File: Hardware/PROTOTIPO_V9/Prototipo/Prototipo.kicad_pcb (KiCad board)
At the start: 2 copper layers, 3 parts

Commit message: Planteo de PCBs
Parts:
- removed REF**: ILI9341, footprints_proyecto:ILI9341
- removed REF**: W5500_ETHERNET_SHIELD, footprints_proyecto:W5500_ETHERNET_SHIELD
- removed REF**: BluePill, footprints_proyecto:YAAJ_BluePill_1
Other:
- board outline added: 204.9 x 224.8 mm
- board text added: "PCB BACK"
- board text added: "PCB FRONT"
- board text added: "Trabajar con grilla 2,54 mm"

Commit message: fp definitivos - Planteo de PCB con componentes
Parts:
- added C1: 100n, Capacitor_THT:CP_Radial_Tantal_D4.5mm_P5.00mm, F.Cu at (214.7, 84.8)
- added C2: 10u, Capacitor_THT:CP_Radial_D5.0mm_P2.50mm, F.Cu at (223.6, 83.8)
- added C3: 10u, Capacitor_THT:CP_Radial_D5.0mm_P2.50mm, F.Cu at (229.7, 115.1)
- added C4: 10u, Capacitor_THT:CP_Radial_D5.0mm_P2.50mm, F.Cu at (246.4, 95.4)
- added J1: Screw_Terminal_01x02, TerminalBlock:TerminalBlock_Xinya_XY308-2.54-2P_1x02_P2.54mm_Horizontal, F.Cu at (165.1, 121.9)
- added J4: Conn_01x10, Connector_PinSocket_2.54mm:PinSocket_2x05_P2.54mm_Vertical, F.Cu at (154.9, 190.5)
- added J5: Conn_01x10, Connector_PinSocket_2.54mm:PinSocket_2x05_P2.54mm_Vertical, F.Cu at (190.5, 86.4)
- added J6: Conn_01x01, Connector_PinHeader_2.54mm:PinHeader_1x01_P2.54mm_Vertical, F.Cu at (237.2, 124.5)
- added J7: Conn_01x01, Connector_PinHeader_2.54mm:PinHeader_1x01_P2.54mm_Vertical, F.Cu at (241.8, 124.5)
- added J8: Conn_01x01, Connector_PinHeader_2.54mm:PinHeader_1x01_P2.54mm_Vertical, F.Cu at (246.4, 124.5)
- added PS1: HLK-5M05, Converter_ACDC:Converter_ACDC_Hi-Link_HLK-5Mxx, F.Cu at (173.7, 50.4)
- added R1: 100, Resistor_THT:R_Axial_DIN0207_L6.3mm_D2.5mm_P10.16mm_Horizontal, F.Cu at (96.2, 249.7)
- added R10: 10k, Resistor_THT:R_Axial_DIN0207_L6.3mm_D2.5mm_P10.16mm_Horizontal, F.Cu at (132.7, 249.7)
- added R11: 10k, Resistor_THT:R_Axial_DIN0207_L6.3mm_D2.5mm_P10.16mm_Horizontal, F.Cu at (136.7, 249.7)
- added R12: 10k, Resistor_THT:R_Axial_DIN0207_L6.3mm_D2.5mm_P10.16mm_Horizontal, F.Cu at (140.8, 249.7)
- added R13: 10k, Resistor_THT:R_Axial_DIN0207_L6.3mm_D2.5mm_P10.16mm_Horizontal, F.Cu at (194.7, 128.2)
- added R14: 10k, Resistor_THT:R_Axial_DIN0207_L6.3mm_D2.5mm_P10.16mm_Horizontal, F.Cu at (215.9, 113.8)
- added R15: 10K, Resistor_THT:R_Axial_DIN0207_L6.3mm_D2.5mm_P10.16mm_Horizontal, F.Cu at (215.9, 117.9)
- added R16: 100, Resistor_THT:R_Axial_DIN0207_L6.3mm_D2.5mm_P10.16mm_Horizontal, F.Cu at (215.9, 121.9)
- added R17: 10k, Resistor_THT:R_Axial_DIN0207_L6.3mm_D2.5mm_P10.16mm_Horizontal, F.Cu at (243.3, 102.6)
- added R18: 10K, Resistor_THT:R_Axial_DIN0207_L6.3mm_D2.5mm_P10.16mm_Horizontal, F.Cu at (243.3, 106.7)
- added R2: 4k7, Resistor_THT:R_Axial_DIN0207_L6.3mm_D2.5mm_P10.16mm_Horizontal, F.Cu at (100.3, 249.7)
- added R3: 4k7, Resistor_THT:R_Axial_DIN0207_L6.3mm_D2.5mm_P10.16mm_Horizontal, F.Cu at (104.3, 249.7)
- added R4: 4k7, Resistor_THT:R_Axial_DIN0207_L6.3mm_D2.5mm_P10.16mm_Horizontal, F.Cu at (108.4, 249.7)
- added R5: 4k7, Resistor_THT:R_Axial_DIN0207_L6.3mm_D2.5mm_P10.16mm_Horizontal, F.Cu at (112.4, 249.7)
- added R6: 4k7, Resistor_THT:R_Axial_DIN0207_L6.3mm_D2.5mm_P10.16mm_Horizontal, F.Cu at (116.5, 249.7)
- added R7: 4k7, Resistor_THT:R_Axial_DIN0207_L6.3mm_D2.5mm_P10.16mm_Horizontal, F.Cu at (120.5, 249.7)
- added R8: 10k, Resistor_THT:R_Axial_DIN0207_L6.3mm_D2.5mm_P10.16mm_Horizontal, F.Cu at (124.6, 249.7)
- added R9: 10k, Resistor_THT:R_Axial_DIN0207_L6.3mm_D2.5mm_P10.16mm_Horizontal, F.Cu at (128.6, 249.7)
- added U1: YAAJ_BluePill_Part_Like_SWD_Breakout, footprints_proyecto:YAAJ_BluePill_1, F.Cu at (269.2, 76.2)
- added U10: ADS1115IDGS, footprints_proyecto:MODULE_ADS1115, F.Cu at (199.4, 114.5)
- added U2: zmpt101b, footprints_proyecto:MODULE_ZMPT101B, F.Cu at (163.8, 101.6)
- added U5: LD1117V33, Package_TO_SOT_THT:TO-220-3_Vertical, F.Cu at (210.8, 73.7)
- added U6: 3013, footprints_proyecto:MODULE_3013, F.Cu at (238.8, 58.4)
- added U7: KY-040, footprints_proyecto:MODULE_KY-040, F.Cu at (175.3, 177.8)
- added U8: W5500_ETHERNET_SHIELD, footprints_proyecto:W5500_ETHERNET_SHIELD, F.Cu at (94.0, 118.4)
- added U9: CR2013-MI2120, Display:CR2013-MI2120, F.Cu at (104.9, 235.4)
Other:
- board size 204.9 x 224.8 mm -> 204.9 x 223.9 mm

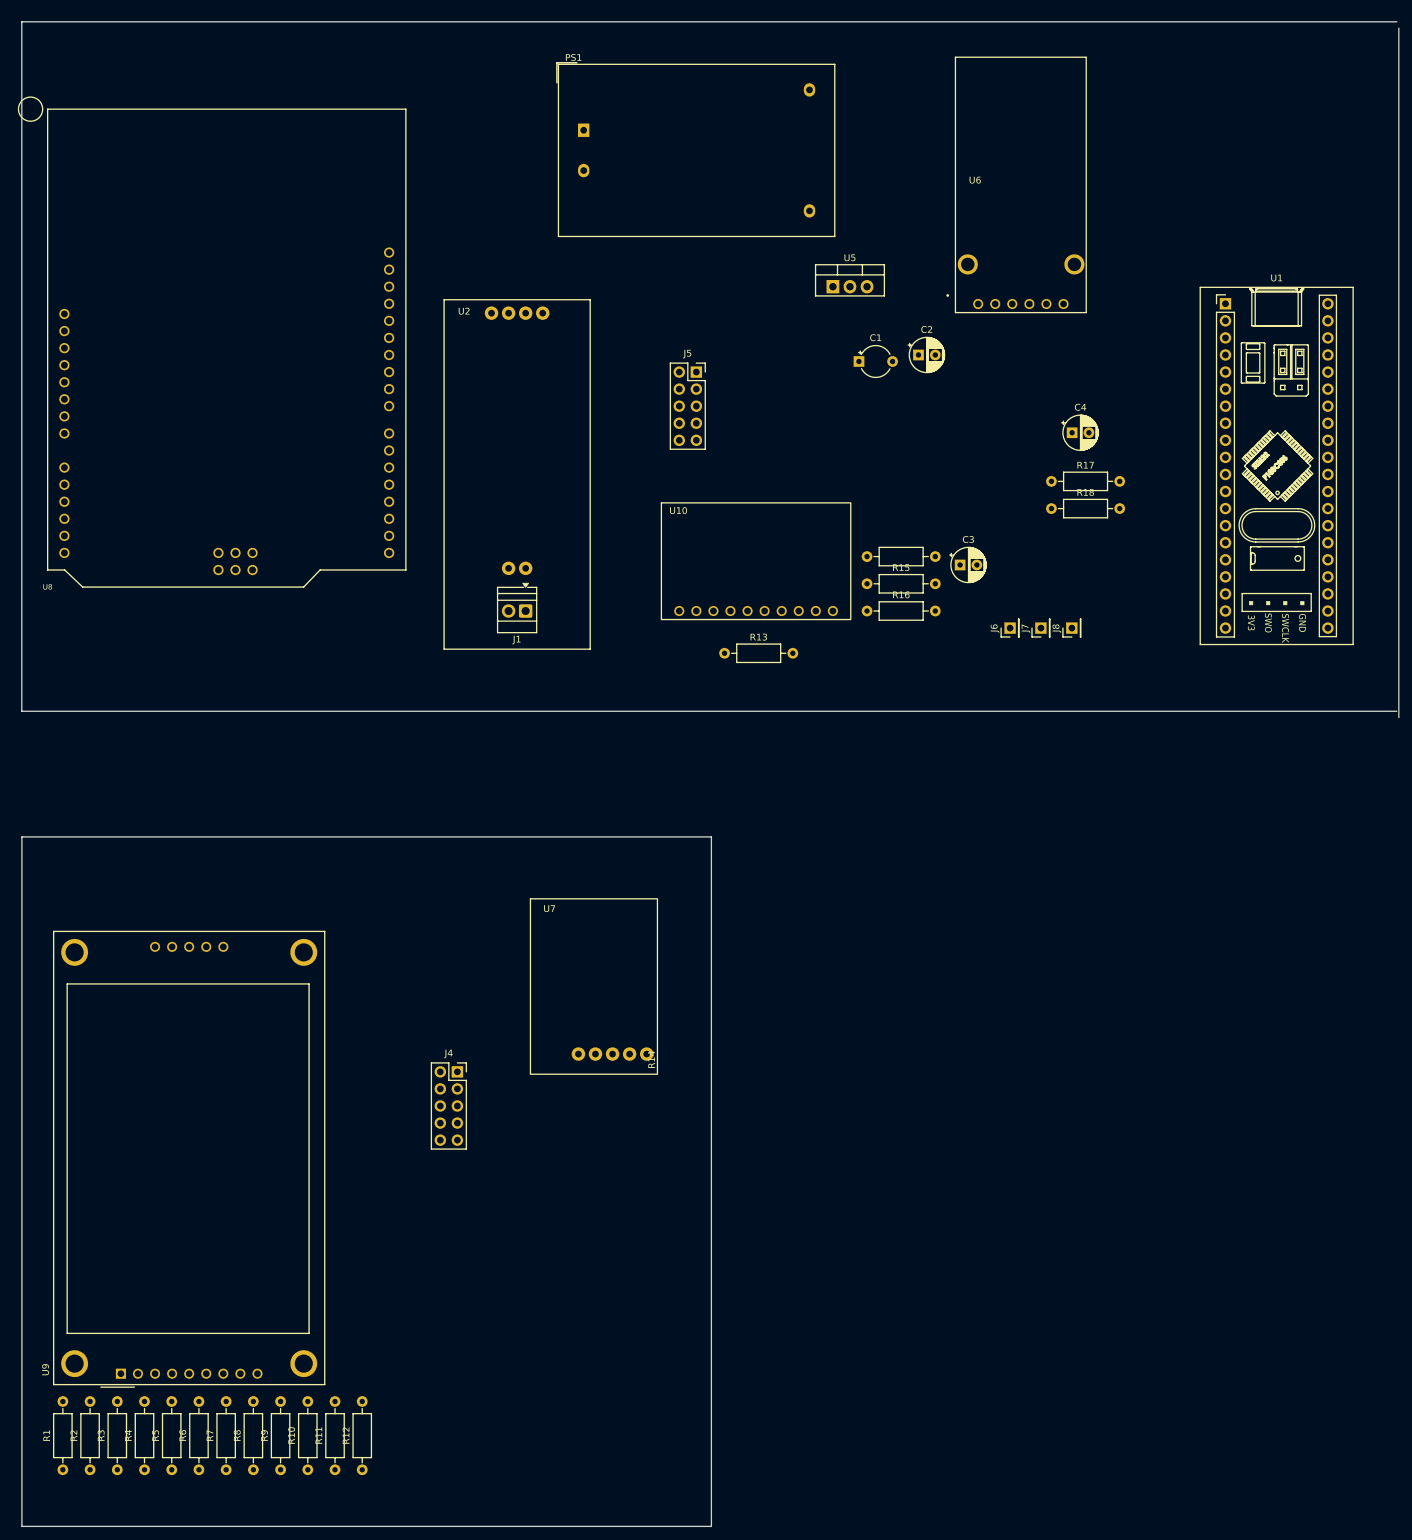
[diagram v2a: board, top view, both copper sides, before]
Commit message: Ruteo de PCB Superior
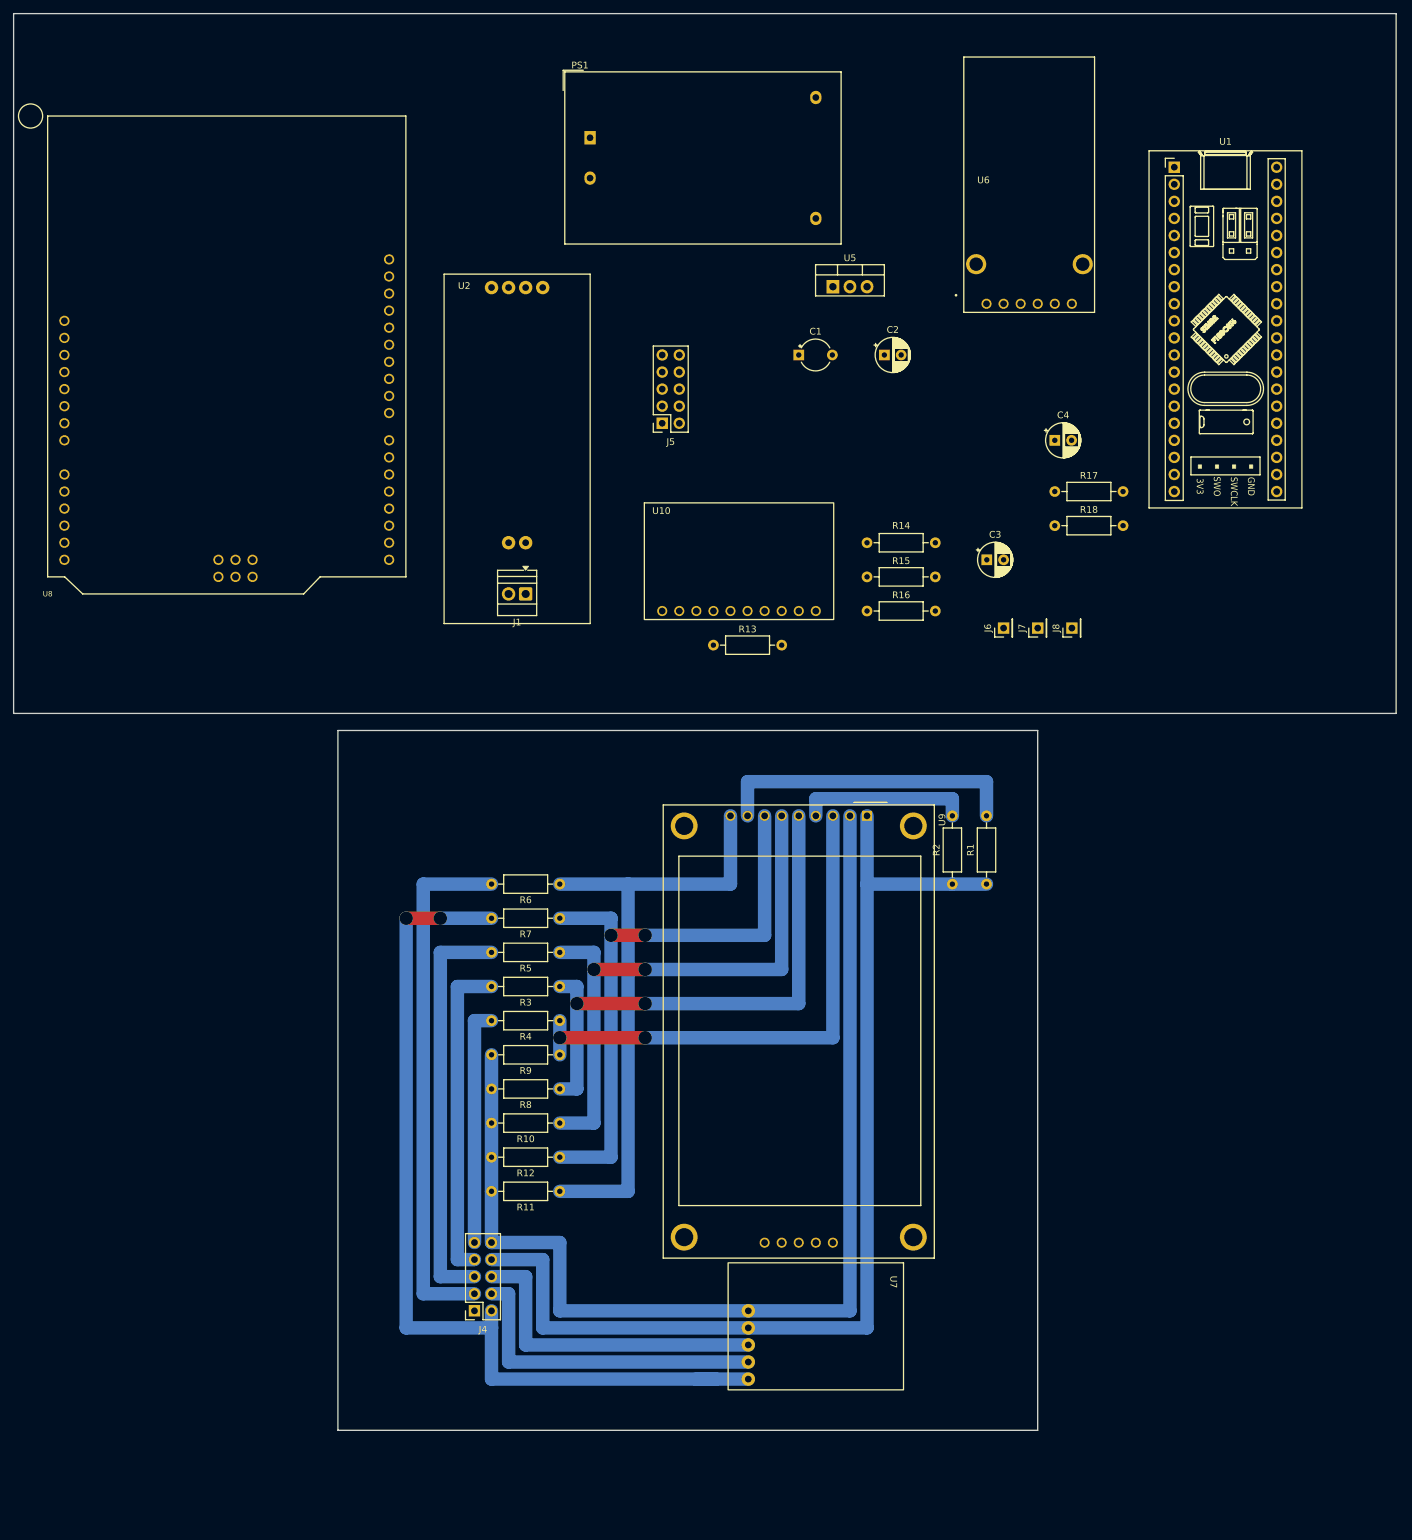
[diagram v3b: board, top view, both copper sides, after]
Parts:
- moved R1 162.8 mm to (233.7, 162.6)
- moved R2 155.1 mm to (228.6, 162.6)
- moved U9 138.6 mm to (215.9, 152.4), turned to -90 degrees
- moved R6 102.4 mm to (170.2, 162.6), turned to 180 degrees
- moved R3 97.5 mm to (170.2, 177.8), turned to 180 degrees
- moved R5 96.2 mm to (170.2, 172.7), turned to 180 degrees
- moved R7 95.9 mm to (170.2, 167.6), turned to 180 degrees
- moved R4 91.0 mm to (170.2, 182.9), turned to 180 degrees
- moved R9 74.4 mm to (170.2, 188.0), turned to 180 degrees
- moved R8 72.7 mm to (170.2, 193.0), turned to 180 degrees
- moved R10 63.8 mm to (170.2, 198.1), turned to 180 degrees
- moved U7 60.4 mm to (208.3, 228.4), turned to -90 degrees
- moved R12 55.0 mm to (170.2, 203.2), turned to 180 degrees
- moved R11 53.3 mm to (170.2, 208.3), turned to 180 degrees
- moved J4 35.7 mm to (157.5, 226.1), turned to 180 degrees
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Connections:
- J4 pad 1: +5V -> unconnected-(J4-Pin_1-Pad1)
- J4 pad 2: /PCB2CONNECTION/ENC_SW -> /PCB2CONNECTION/CLK
- J4 pad 3: /PCB2CONNECTION/ENC_DT -> /PCB2CONNECTION/LCD_MISO
- J4 pad 4: /PCB2CONNECTION/ENC_CLK -> /PCB2CONNECTION/ENC_DT
- J4 pad 5: unconnected-(J4-Pin_5-Pad5) -> /PCB2CONNECTION/LCD_MOSI
- J4 pad 6: /PCB2CONNECTION/LCD_CS -> /PCB2CONNECTION/ENC_SW
- J4 pad 8: /PCB2CONNECTION/LCD_MISO -> +5V
- J4 pad 9: /PCB2CONNECTION/LCD_MOSI -> /PCB2CONNECTION/LCD_CS
- J5 pad 1: +5V -> unconnected-(J5-Pin_1-Pad1)
- J5 pad 2: /PCB2CONNECTION/BUS_ENC_SW -> /PCB2CONNECTION/BUS_ENC_CLK
- J5 pad 3: /PCB2CONNECTION/BUS_ENC_DT -> MISO
- J5 pad 4: /PCB2CONNECTION/BUS_ENC_CLK -> /PCB2CONNECTION/BUS_ENC_DT
- J5 pad 5: unconnected-(J5-Pin_5-Pad5) -> MOSI
- J5 pad 6: /PCB2CONNECTION/BUS_LCD_CS -> /PCB2CONNECTION/BUS_ENC_SW
- J5 pad 8: MISO -> +5V
- J5 pad 9: MOSI -> /PCB2CONNECTION/BUS_LCD_CS
- R7 pad 2: /PCB2CONNECTION/ENC_CLK -> /PCB2CONNECTION/CLK
- U7 pad CLK: /PCB2CONNECTION/ENC_CLK -> /PCB2CONNECTION/CLK
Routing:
- net GND: track 0.00 -> 165.1 mm
- net +5V: track 0.00 -> 160.0 mm
- net /PCB2CONNECTION/CLK: track 0.00 -> 137.6 mm, vias 0 -> 2
- net Net-(U9-SCK): track 0.00 -> 91.4 mm, vias 0 -> 2
- net Net-(U9-MISO): track 0.00 -> 91.4 mm
- net Net-(U9-MOSI): track 0.00 -> 86.4 mm, vias 0 -> 2
- net Net-(U9-D/~{C}): track 0.00 -> 81.3 mm, vias 0 -> 2
- net Net-(U9-~{CS}): track 0.00 -> 78.7 mm, vias 0 -> 2
- net /PCB2CONNECTION/LCD_MISO: track 0.00 -> 78.7 mm
- net /PCB2CONNECTION/LCD_MOSI: track 0.00 -> 61.0 mm
- net /PCB2CONNECTION/ENC_SW: track 0.00 -> 48.4 mm
- net /PCB2CONNECTION/ENC_DT: track 0.00 -> 48.4 mm
- net /PCB2CONNECTION/LCD_DC: track 0.00 -> 48.3 mm
- net Net-(U9-LED): track 0.00 -> 45.7 mm
- net /PCB2CONNECTION/LCD_CS: track 0.00 -> 35.6 mm
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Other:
- board size 204.9 x 223.9 mm -> 205.7 x 210.8 mm
- board text added: "+5V"
- board text added: "CLK"
- board text added: "CS"
- board text added: "DC"
- board text added: "DT"
- board text added: "GND"
- board text added: "MISO"
- board text added: "MOSI"
- board text added: "SW"
- board text added: "Trabajar con grilla 2,54 mm, curvas a 90°, en capa back"
- board text removed: "Trabajar con grilla 2,54 mm"

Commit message: Migración de sch a BlackPill
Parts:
- removed R1: 100, Resistor_THT:R_Axial_DIN0207_L6.3mm_D2.5mm_P10.16mm_Horizontal
- removed R10, R11, R12, R8, R9: 10k, Resistor_THT:R_Axial_DIN0207_L6.3mm_D2.5mm_P10.16mm_Horizontal
- removed R2, R3, R4, R5, R6, R7: 4k7, Resistor_THT:R_Axial_DIN0207_L6.3mm_D2.5mm_P10.16mm_Horizontal
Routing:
- net GND: track 165.1 -> 144.8 mm
- net Net-(U9-D/~{C}): track 81.3 -> 61.0 mm, vias 2 -> 1
- net Net-(U9-~{CS}): track 78.7 -> 73.7 mm, vias 2 -> 1
- net /PCB2CONNECTION/LCD_CS: track 35.6 -> 33.0 mm

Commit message: Shc final y ruteo de PCB
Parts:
- removed C4: 10u, Capacitor_THT:CP_Radial_D5.0mm_P2.50mm
- removed R13, R17: 10k, Resistor_THT:R_Axial_DIN0207_L6.3mm_D2.5mm_P10.16mm_Horizontal
- removed R18: 10K, Resistor_THT:R_Axial_DIN0207_L6.3mm_D2.5mm_P10.16mm_Horizontal
- removed U1: YAAJ_BluePill_Part_Like_SWD_Breakout, footprints_proyecto:YAAJ_BluePill_1
- added JP1: Jumper_2_Bridged, Connector_PinHeader_2.54mm:PinHeader_1x02_P2.54mm_Vertical, F.Cu at (226.1, 119.4)
- added JP2: Jumper_2_Bridged, Connector_PinHeader_2.54mm:PinHeader_1x02_P2.54mm_Vertical, F.Cu at (223.5, 119.4)
- added JP3: Jumper_2_Bridged, Connector_PinHeader_2.54mm:PinHeader_1x02_P2.54mm_Vertical, F.Cu at (241.3, 119.4)
- added JP4: Jumper_2_Bridged, Connector_PinHeader_2.54mm:PinHeader_1x02_P2.54mm_Vertical, F.Cu at (238.8, 119.4)
- added R1: 100, Resistor_THT:R_Axial_DIN0207_L6.3mm_D2.5mm_P10.16mm_Horizontal, F.Cu at (200.7, 147.3)
- added R5: 1K5, Resistor_THT:R_Axial_DIN0207_L6.3mm_D2.5mm_P10.16mm_Horizontal, F.Cu at (251.5, 101.6)
- added R6: 1K5, Resistor_THT:R_Axial_DIN0207_L6.3mm_D2.5mm_P10.16mm_Horizontal, F.Cu at (248.9, 101.6)
- added U3: YAAJ_BlackPill_Part_Like_SWD_Breakout, footprints_proyecto:YAAJ_BlackPill_SWD_1, F.Cu at (195.6, 96.5)
- J4, J5: value Conn_01x10 -> Conn_02x06_Counter_Clockwise; footprint Connector_PinSocket_2.54mm:PinSocket_2x05_P2.54mm_Vertical -> Connector_PinSocket_2.54mm:PinSocket_2x06_P2.54mm_Vertical
- moved J1 102.4 mm to (238.8, 48.2), turned to 0 degrees
- moved PS1 98.1 mm to (272.7, 48.3), turned to -90 degrees
- moved U5 81.8 mm to (284.5, 109.2), turned to 90 degrees
- moved U2 81.2 mm to (240.0, 69.8), turned to 180 degrees
- moved J6 78.9 mm to (215.9, 48.2), turned to 180 degrees
- moved J7 78.9 mm to (221.0, 48.2), turned to 180 degrees
- moved J8 78.8 mm to (218.4, 50.8), turned to 180 degrees
- moved C1 77.3 mm to (281.9, 96.5), turned to 90 degrees
- moved C2 71.6 mm to (281.9, 116.9), turned to -90 degrees
- moved R2 66.5 mm to (223.5, 55.8), turned to 180 degrees
- moved U6 56.9 mm to (265.5, 109.2), turned to 180 degrees
- moved R4 51.4 mm to (223.5, 60.9), turned to 180 degrees
- moved R3 50.9 mm to (213.4, 66.0)
- moved C3 45.4 mm to (213.4, 73.7)
- moved J5 39.7 mm to (160.0, 63.5), turned to 0 degrees
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- renumbered R16 to R2, R15 to R3, R14 to R4
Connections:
- J4 pad 1: unconnected-(J4-Pin_1-Pad1) -> /PCB2CONNECTION/ENC_CLK
- J4 pad 10: GND -> /PCB2CONNECTION/LCD_CS
- J4 pad 2: /PCB2CONNECTION/CLK -> /PCB2CONNECTION/ENC_DT
- J4 pad 3: /PCB2CONNECTION/LCD_MISO -> unconnected-(J4-Pin_2-Pad3)
- J4 pad 4: /PCB2CONNECTION/ENC_DT -> /PCB2CONNECTION/ENC_SW
- J4 pad 5: /PCB2CONNECTION/LCD_MOSI -> /PCB2CONNECTION/LCD_MISO
- J4 pad 6: /PCB2CONNECTION/ENC_SW -> /PCB2CONNECTION/+5V_
- J4 pad 7: /PCB2CONNECTION/LCD_DC -> /PCB2CONNECTION/LCD_SCK
- J4 pad 8: +5V -> /PCB2CONNECTION/GND_
- J4 pad 9: /PCB2CONNECTION/LCD_CS -> /PCB2CONNECTION/LCD_MOSI
- J5 pad 1: unconnected-(J5-Pin_1-Pad1) -> /PCB2CONNECTION/BUS_ENC_CLK
- J5 pad 10: GND -> /PCB2CONNECTION/BUS_LCD_CS
- J5 pad 2: /PCB2CONNECTION/BUS_ENC_CLK -> /PCB2CONNECTION/BUS_ENC_DT
- J5 pad 3: MISO -> unconnected-(J5-Pin_2-Pad3)
- J5 pad 4: /PCB2CONNECTION/BUS_ENC_DT -> /PCB2CONNECTION/BUS_ENC_SW
- J5 pad 5: MOSI -> MISO
- J5 pad 6: /PCB2CONNECTION/BUS_ENC_SW -> +5V
- J5 pad 7: /PCB2CONNECTION/BUS_LCD_DC -> SCK
- J5 pad 8: +5V -> GND
- J5 pad 9: /PCB2CONNECTION/BUS_LCD_CS -> MOSI
- R4 pad 1: +5V -> +3V3
- U10 pad 5: /ADS1115/ADC_IN1 -> /SCT013_100A_1V/TOP
- U10 pad 6: /SCT013_100A_1V/TOP -> unconnected-(U10-AIN2-Pad6)
- U10 pad 7: /SCT013_100A_1V/RING -> unconnected-(U10-AIN3-Pad7)
- U10 pad 8: +5V -> +3V3
- U2 pad 5: +5V -> +3V3
- U7 pad CLK: /PCB2CONNECTION/CLK -> /PCB2CONNECTION/ENC_CLK
- U7 pad GND: GND -> /PCB2CONNECTION/GND_
- U7 pad VCC: +5V -> /PCB2CONNECTION/+5V_
- U9 pad 1: +5V -> /PCB2CONNECTION/+5V_
- U9 pad 2: GND -> /PCB2CONNECTION/GND_
- U9 pad 3: Net-(U9-~{CS}) -> /PCB2CONNECTION/LCD_CS
- U9 pad 4: Net-(U9-RESET) -> /PCB2CONNECTION/LCD_RST
- U9 pad 5: Net-(U9-D/~{C}) -> /PCB2CONNECTION/LCD_DC
- U9 pad 6: Net-(U9-MOSI) -> /PCB2CONNECTION/LCD_MOSI
- U9 pad 7: Net-(U9-SCK) -> /PCB2CONNECTION/LCD_SCK
- U9 pad 9: Net-(U9-MISO) -> /PCB2CONNECTION/LCD_MISO
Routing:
- net GND: track 144.8 -> 517.7 mm, vias 0 -> 6
- net +5V: track 160.0 -> 384.6 mm, vias 0 -> 6
- net /DS3231/RTC_SCL: track 0.00 -> 193.1 mm, vias 0 -> 4
- net /PCB2CONNECTION/BUS_LCD_RST: track 0.00 -> 188.0 mm, vias 0 -> 8
- net /DS3231/RTC_SDA: track 0.00 -> 177.8 mm, vias 0 -> 4
- net /W5500/Eth_RST: track 0.00 -> 170.2 mm, vias 0 -> 8
- net +3V3: track 0.00 -> 152.4 mm, vias 0 -> 2
- net /PCB2CONNECTION/BUS_ENC_SW: track 0.00 -> 144.8 mm, vias 0 -> 8
- net /PCB2CONNECTION/CLK: track 137.6 -> 0.00 mm, vias 2 -> 0
- net /PCB2CONNECTION/+5V_: track 0.00 -> 129.5 mm
- net /PCB2CONNECTION/GND_: track 0.00 -> 116.8 mm
- net /PCB2CONNECTION/LCD_SCK: track 0.00 -> 116.8 mm
- net /PCB2CONNECTION/LCD_RST: track 0.00 -> 106.7 mm
- net Net-(U9-SCK): track 91.4 -> 0.00 mm, vias 2 -> 0
- net Net-(U9-MISO): track 91.4 -> 0.00 mm
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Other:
- board text added: "BACK PCB"
- board text added: "FRONT PCB"
- board text added: "MCEE_v1_2026"
- board text added: "UTN FRH - Proyecto Final de Ing Electrónica"
- board text removed: "+5V"
- board text removed: "CLK"
- board text removed: "CS"
- board text removed: "DC"
- board text removed: "DT"
- board text removed: "GND"
- board text removed: "MISO"
- board text removed: "MOSI"
- board text removed: "PCB BACK"
- board text removed: "PCB FRONT"
- board text removed: "SW"
- board text removed: "Trabajar con grilla 2,54 mm, curvas a 90°, en capa back"
